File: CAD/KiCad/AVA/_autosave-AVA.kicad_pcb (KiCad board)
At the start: 2 copper layers, 100 x 75 mm, 48 parts, among them J1 Conn_01x03_Pin, J10 Conn_01x04_Pin, J2 Conn_01x03_Pin, J3 Conn_01x03_Pin, J4 Conn_01x03_Pin, J5 Conn_01x02_Pin, J6 Conn_01x02_Pin, J7 Conn_01x02_Pin, J8 Conn_01x03_Pin, J9 Conn_01x03_Pin, U1 ESP32-C3-Super-Mini, U2 ESP32-DevKitC

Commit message: :D
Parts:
- moved R18 11.4 mm to (179.7, 82.5), turned to 180 degrees
- moved R21 7.62 mm to (169.5, 79.4)
- moved R19 4.44 mm to (169.5, 76.2)
- moved R20 1.91 mm to (169.5, 85.7)
- moved R27 0.63 mm to (166.4, 93.3)
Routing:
- net Net-(U2-GPIO21): track 3.17 -> 70.8 mm
- net Net-(U2-GPIO5): track 0.00 -> 53.5 mm
- net Net-(U2-GPIO19): track 3.17 -> 54.3 mm
- net Net-(U1-3.3V): track 0.00 -> 50.3 mm
- net VCC: track 23.0 -> 64.7 mm
- net Net-(U2-GPIO18): track 0.00 -> 40.5 mm
- net /6.2V: track 24.5 -> 62.2 mm
- net Net-(U2-GPIO22): track 0.00 -> 15.5 mm
- net Net-(U2-GPIO23): track 0.00 -> 8.06 mm
- net /CH1: track 0.00 -> 6.77 mm
- net Net-(J7-Pin_2): track 0.00 -> 6.61 mm
- net Net-(J7-Pin_1): track 0.00 -> 6.61 mm
- net /CH2: track 0.00 -> 6.24 mm

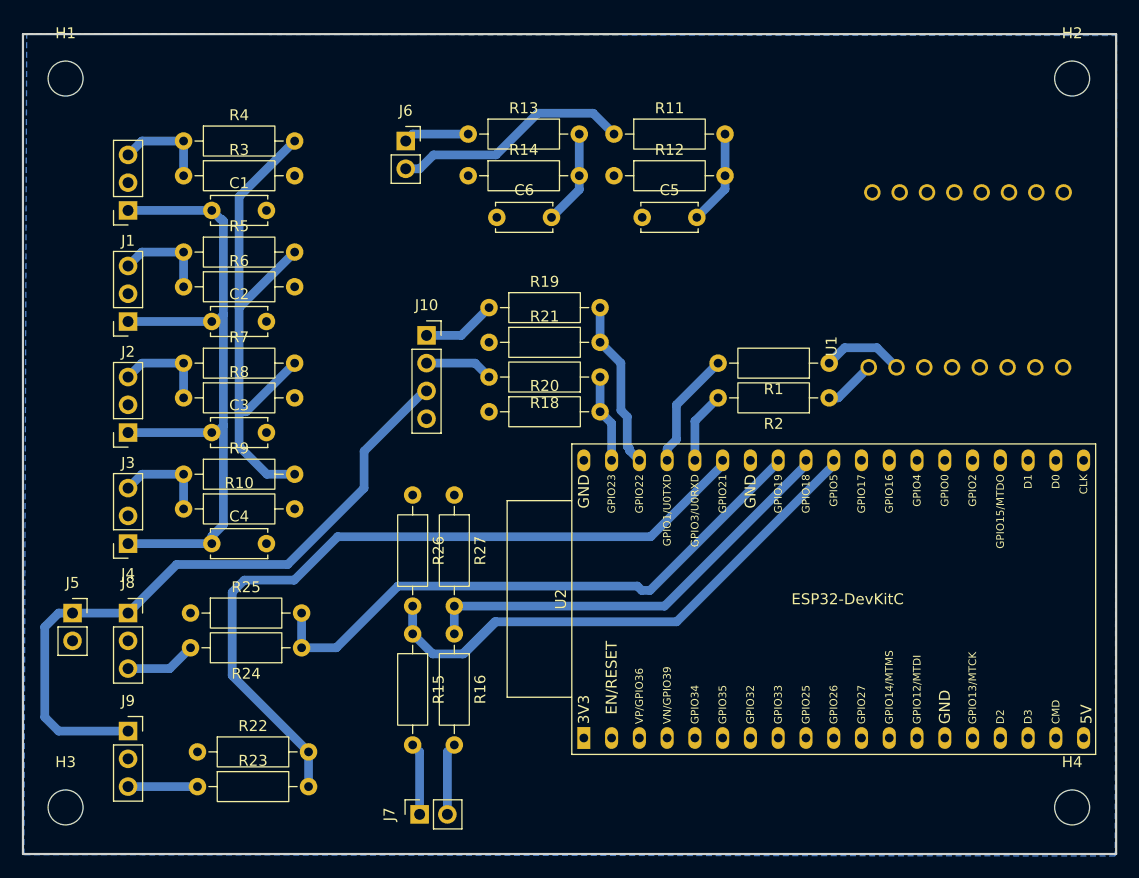
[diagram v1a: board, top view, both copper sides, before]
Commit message: Modern PCB-CAD software requires 7GB of RAM to open a window. Where did we go wrong. Layout finished
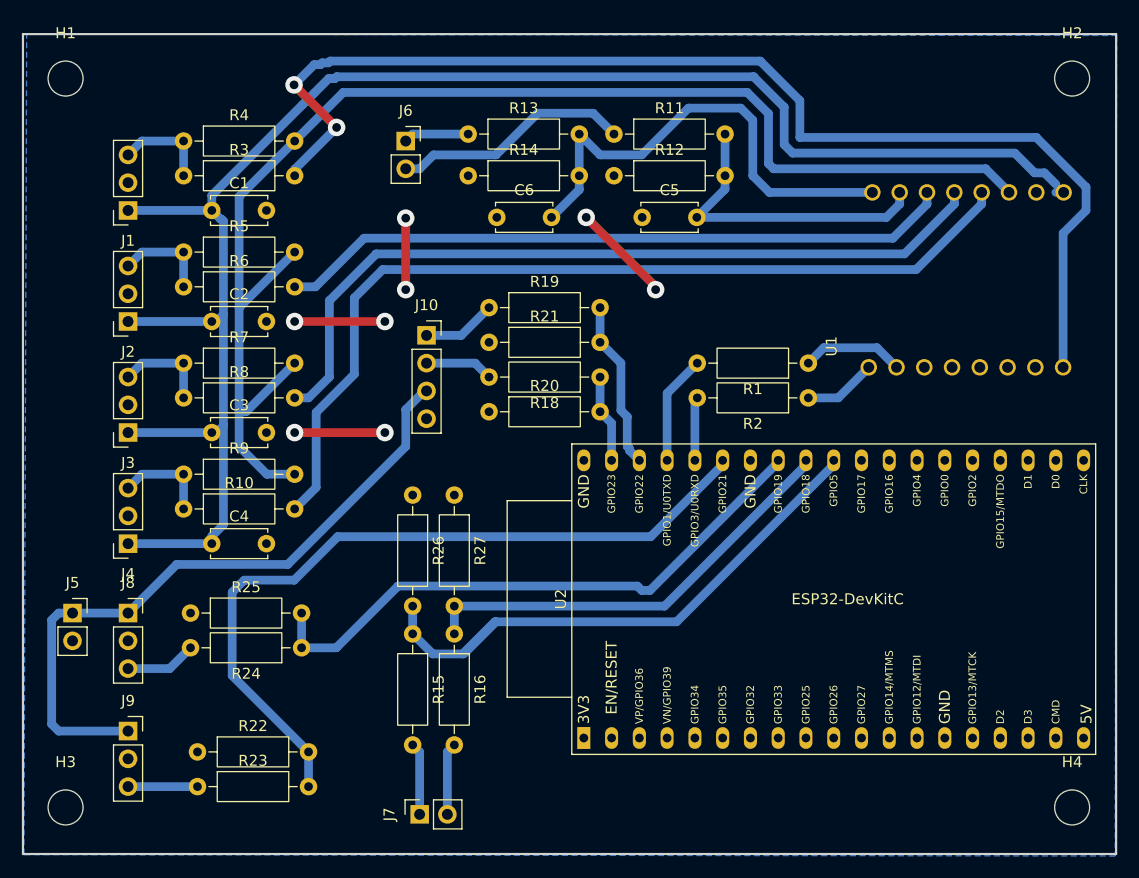
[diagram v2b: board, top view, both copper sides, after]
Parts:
- moved R1 1.91 mm to (198.8, 81.3)
- moved R2 1.91 mm to (198.8, 84.5)
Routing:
- net Net-(U1-PISO/GPIO5): track 0.00 -> 109.0 mm, vias 0 -> 2
- net VCC: track 64.7 -> 154.6 mm
- net Net-(U1-SCLK/A4/GPIO4): track 0.00 -> 83.6 mm
- net Net-(U1-3.3V): track 50.3 -> 124.0 mm
- net Net-(U1-A3/GPIO3): track 0.00 -> 72.8 mm
- net Net-(U1-A2/GPIO2): track 0.00 -> 62.0 mm
- net Net-(U1-A0/GPIO0): track 8.67 -> 44.2 mm
- net GND: track 0.00 -> 32.3 mm, vias 0 -> 8
- net Net-(U1-A1/GPIO1): track 8.69 -> 28.8 mm
- net Net-(U1-TX/GPIO21): track 4.78 -> 6.68 mm
- net Net-(U1-RX/GPIO20): track 7.48 -> 9.39 mm
- net Net-(U2-U0RXD/GPIO3): track 6.59 -> 5.81 mm
- net Net-(U2-U0TXD/GPIO1): track 10.8 -> 10.0 mm
- net /6.2V: track 62.2 -> 61.7 mm
